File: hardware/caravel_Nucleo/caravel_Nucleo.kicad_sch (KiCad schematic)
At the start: 65 parts, among them J1 10118193-0001LF, J10 PinHeader_1x11, J11 PinHeader_1x02, J12 PinHeader_1x02, J3 PinHeader_1x02, J4 836-22-004-10-001101, J5 PinHeader_1x02, J6 PinHeader_1x02, J7 836-22-006-10-001101, J8 640456-3, J9 640456-3, SW1 KMR2, T1 Logo, T2 Logo, U10 MCP4661, U12 NUCLEO144-F746ZG, U4 MAX811REUS+T, U5 TAR5S33UTE85LF, U6 TAR5S18U(TE85L,F), U7 W25Q32FVSS, U8 caravel_breakout, U9 MIC2211-AAYML-TR, X1 ECS-2520MVLC-100-BN-TR

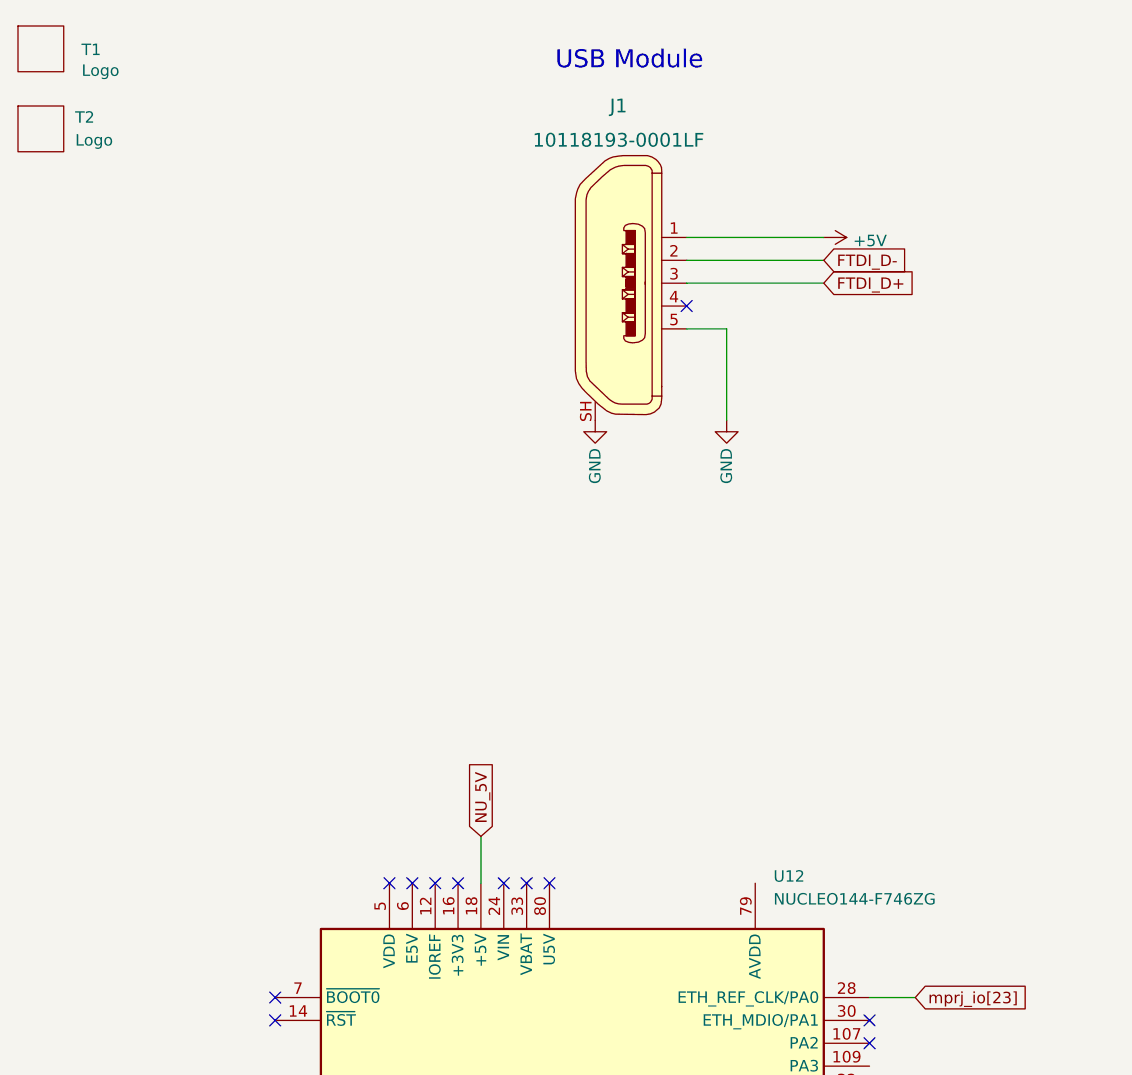
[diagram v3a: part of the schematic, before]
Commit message: Move components to local library
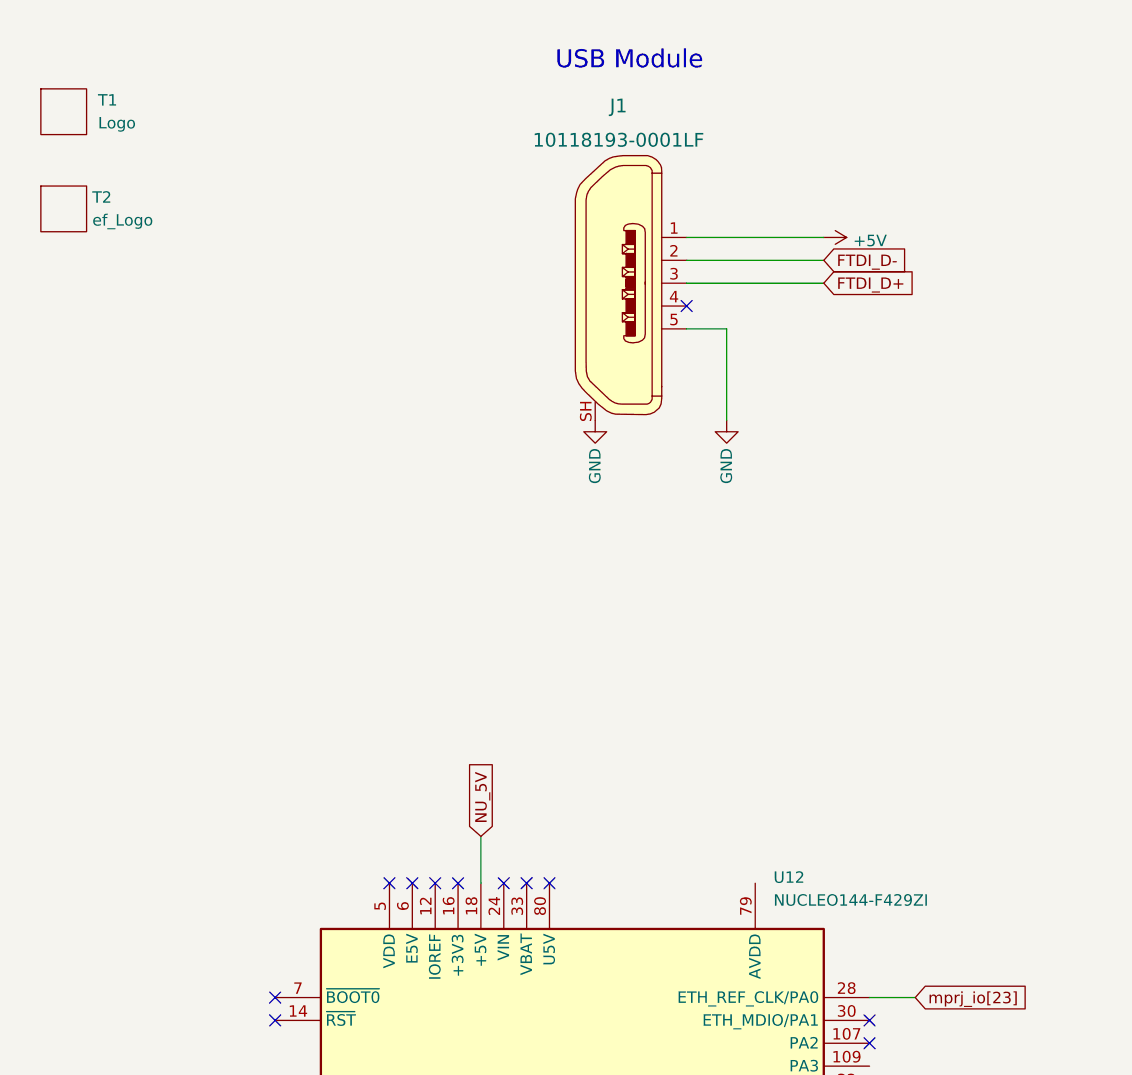
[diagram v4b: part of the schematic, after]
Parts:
- removed T1: Logo, Caravel_Board:logo, symbol Caravel_board:Logo
- removed T2: Logo, Caravel_Board:ef_logo, symbol Caravel_board:Logo
- removed U12: NUCLEO144-F746ZG, Module:ST_Morpho_Connector_144_STLink, symbol MCU_Module:NUCLEO144-F746ZG
- added T1: Logo, caravel_Nucleo-footprints:logo, symbol caravel_Nucleo:Logo
- added T2: ef_Logo, caravel_Nucleo-footprints:ef_logo, symbol caravel_Nucleo:ef_Logo
- added U12: NUCLEO144-F429ZI, caravel_Nucleo-footprints:ST_Morpho_Connectors_144, symbol caravel_Nucleo:NUCLEO144-F429ZI
- C10, C13, C18, C20, C21: footprint antmicro-footprints:0603-cap -> caravel_Nucleo-footprints:0603-cap; symbol antmicroCapacitors0603:C_1u_0603 -> caravel_Nucleo:C_1u_0603
- C11, C14, C19: footprint antmicro-footprints:0603-cap -> caravel_Nucleo-footprints:0603-cap; symbol antmicroCapacitors0603:C_10n_0603 -> caravel_Nucleo:C_10n_0603
- C12, C15: footprint antmicro-footprints:0603-cap -> caravel_Nucleo-footprints:0603-cap; symbol antmicroCapacitors0603:C_10u_0603 -> caravel_Nucleo:C_10u_0603
- C16, C17, C9: footprint antmicro-footprints:0603-cap -> caravel_Nucleo-footprints:0603-cap; symbol antmicroCapacitors0603:C_100n_0603 -> caravel_Nucleo:C_100n_0603
- D3, D4: footprint antmicro-footprints:LED-1206 -> caravel_Nucleo-footprints:LED-1206; symbol antmicroLEDIndicationDiscrete:LTST-C150KGKT -> caravel_Nucleo:LTST-C150KGKT
- J1: footprint antmicro-footprints:USB_Micro_B_Female_10118193-0001LF -> caravel_Nucleo-footprints:USB_Micro_B_Female_10118193-0001LF; symbol antmicroUSBDVIHDMIConnectors:10118193-0001LF -> caravel_Nucleo:10118193-0001LF
- J10: footprint antmicro-footprints:PinHeader_1x11_P2.54_Vertical -> caravel_Nucleo-footprints:PinHeader_1x11_P2.54_Vertical; symbol antmicroRectangularConnectorsHeadersMalePins:PinHeader_1x11 -> caravel_Nucleo:PinHeader_1x11
- J11, J12, J3, J5, J6: footprint antmicro-footprints:PinHeader_1x2_P2.54mm -> caravel_Nucleo-footprints:PinHeader_1x2_P2.54mm; symbol antmicroRectangularConnectorsHeadersMalePins:PinHeader_1x02 -> caravel_Nucleo:PinHeader_1x02
- J4: footprint antmicro-footprints:PogoPinHeader_1x4_P2mm_Drill1,5mm -> caravel_Nucleo-footprints:PogoPinHeader_1x4_P2mm_Drill1,5mm; symbol antmicroRectangularConnectorsHeadersMalePins:836-22-004-10-001101 -> caravel_Nucleo:836-22-004-10-001101
- J7: footprint antmicro-footprints:PogoPinHeader_1x6_P2mm_Drill1,5mm -> caravel_Nucleo-footprints:PogoPinHeader_1x6_P2mm_Drill1,5mm; symbol antmicroRectangularConnectorsHeadersMalePins:836-22-006-10-001101 -> caravel_Nucleo:836-22-006-10-001101
- J8, J9: footprint antmicro-footprints:PinHeader_1x3_P2.54_Drill1.1mm -> caravel_Nucleo-footprints:PinHeader_1x3_P2.54_Drill1.1mm; symbol antmicroRectangularConnectorsHeadersMalePins:640456-3 -> caravel_Nucleo:640456-3
- R10, R11, R12, R15, R16, R17, R18, R27, R7, R8, R9: footprint antmicro-footprints:0603-res -> caravel_Nucleo-footprints:0603-res; symbol antmicroResistors0603:R_10k_0603 -> caravel_Nucleo:R_10k_0603
- R13, R14: footprint antmicro-footprints:0603-res -> caravel_Nucleo-footprints:0603-res; symbol antmicroResistors0603:R_82R_0603 -> caravel_Nucleo:R_82R_0603
- R19: footprint antmicro-footprints:0603-res -> caravel_Nucleo-footprints:0603-res; symbol antmicroResistors0603:R_360R_0603 -> caravel_Nucleo:R_360R_0603
- R20, R23: footprint antmicro-footprints:0603-res -> caravel_Nucleo-footprints:0603-res; symbol antmicroResistors0603:R_4k99_0603 -> caravel_Nucleo:R_4k99_0603
- R21: footprint antmicro-footprints:0603-res -> caravel_Nucleo-footprints:0603-res; symbol antmicroResistors0603:R_499R_0603 -> caravel_Nucleo:R_499R_0603
- R22: footprint antmicro-footprints:0603-res -> caravel_Nucleo-footprints:0603-res; symbol antmicroResistors0603:R_4k22_0603 -> caravel_Nucleo:R_4k22_0603
- R24: footprint antmicro-footprints:0402-res -> caravel_Nucleo-footprints:0402-res; symbol antmicroResistors0402:R_4k02_0402 -> caravel_Nucleo:R_4k02_0402
- R25, R26: footprint antmicro-footprints:0603-res -> caravel_Nucleo-footprints:0603-res; symbol antmicroResistors0603:R_4k7_0603 -> caravel_Nucleo:R_4k7_0603
- R29, R30, R31, R32, R33: footprint antmicro-footprints:0603-res -> caravel_Nucleo-footprints:0603-res; symbol antmicroResistors0603:R_0R_0603 -> caravel_Nucleo:R_0R_0603
- SW1: footprint antmicro-footprints:SW_SPST_4.2x2.8 -> caravel_Nucleo-footprints:SW_SPST_4.2x2.8; symbol antmicroPushbuttonSwitches:KMR2 -> caravel_Nucleo:KMR2
- TP1: footprint antmicro-footprints:Testpoint_smd_1mm -> caravel_Nucleo-footprints:Testpoint_smd_1mm; symbol antmicroTestPoints:TP_SMD1MM -> caravel_Nucleo:TP_SMD1MM
- U10: footprint antmicro-footprints:QFN-16_EP_4x4_Pitch0.65mm -> caravel_Nucleo-footprints:QFN-16_EP_4x4_Pitch0.65mm; symbol antmicroInterfaceIOExpanders:MCP4661 -> caravel_Nucleo:MCP4661
- U4: footprint antmicro-footprints:SOT-143-4 -> caravel_Nucleo-footprints:SOT-143-4; symbol antmicroPMICPowerSequencers:MAX811REUS+T -> caravel_Nucleo:MAX811REUS+T
- U5: footprint antmicro-footprints:SOT-353 -> caravel_Nucleo-footprints:SOT-353; symbol antmicroPMICVoltageRegulatorsLinear:TAR5S33UTE85LF -> caravel_Nucleo:TAR5S33UTE85LF
- U6: footprint antmicro-footprints:SOT-353 -> caravel_Nucleo-footprints:SOT-353; symbol antmicroPMICVoltageRegulatorsLinear:TAR5S18U(TE85L,F) -> caravel_Nucleo:TAR5S18U(TE85L,F)
- U7: footprint antmicro-footprints:SOIC127P790X216-8N -> caravel_Nucleo-footprints:SOIC127P790X216-8N; symbol antmicroMemory:W25Q32FVSS -> caravel_Nucleo:W25Q32FVSS
- U8: footprint antmicro-footprints:caravel_breakout -> caravel_Nucleo-footprints:caravel_breakout; symbol antmicroModules:caravel_breakout -> caravel_Nucleo:caravel_breakout
- U9: footprint antmicro-footprints:DFN-10-1EP_3x3mm -> caravel_Nucleo-footprints:DFN-10-1EP_3x3mm; symbol antmicroPMICVoltageRegulatorsLinear:MIC2211-AAYML-TR -> caravel_Nucleo:MIC2211-AAYML-TR
- X1: footprint antmicro-footprints:Oscillator_SMD_ECS_2520MV-xxx-xx-4Pin_2.5x2.0mm -> caravel_Nucleo-footprints:Oscillator_SMD_ECS_2520MV-xxx-xx-4Pin_2.5x2.0mm; symbol antmicroCrystals:ECS-2520MVLC-100-BN-TR -> caravel_Nucleo:ECS-2520MVLC-100-BN-TR
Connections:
- net EN_VOUT1: now also U12.52 (PF2)
- net EN_VOUT2: now also U12.47 (PE3)
- net GND: now also U12.104 (AGND), U12.111 (GND), U12.126 (GND), U12.135 (GND), U12.143 (GND), U12.144 (GND), U12.19 (GND), U12.20 (GND), U12.22 (GND), U12.49 (GND), U12.60 (GND), U12.71 (GND), U12.72 (GND), U12.8 (GND), U12.81 (GND), U12.92 (GND)
- net I2C4_SCL: now also U12.115 (PD12)
- net I2C4_SDA: now also U12.113 (PD13)
- net NU_5V: now also U12.18 (+5V)
- net SPI4_CS: now also U12.128 (PE11)
- net SPI4_MISO: now also U12.127 (PE13)
- net SPI4_MOSI: now also U12.123 (PE14)
- net SPI4_SCK: now also U12.121 (PE12)
- net SPI5_CS: now also U12.9 (PF6)
- net SPI5_MISO: now also U12.54 (PF8)
- net SPI5_MOSI: now also U12.56 (PF9)
- net SPI5_SCK: now also U12.11 (PF7)
- net TIM3_CH2: now also U12.101 (PB5)
- net UART8_RX: now also U12.136 (PE0)
- net UART8_TX: now also U12.61 (PE1)
- net mprj_io[0]: now also U12.65 (PG12)
- net mprj_io[10]: now also U12.59 (PG0)
- net mprj_io[11]: now also U12.58 (PG1)
- net mprj_io[12]: now also U12.45 (PD7)
- net mprj_io[13]: now also U12.44 (PG3)
- net mprj_io[14]: now also U12.43 (PD6)
- net mprj_io[15]: now also U12.42 (PG2)
- net mprj_io[16]: now also U12.41 (PD5)
- net mprj_io[17]: now also U12.40 (PD3)
- net mprj_io[18]: now also U12.39 (PD4)
- net mprj_io[19]: now also U12.38 (PC0)
- net mprj_io[20]: now also U12.37 (PC3)
- net mprj_io[21]: now also U12.35 (PC2)
- net mprj_io[22]: now also U12.32 (PA4)
- net mprj_io[23]: now also U12.28 (ETH_REF_CLK/PA0)
- net mprj_io[24]: now also U12.17 (PA15)
- net mprj_io[25]: now also U12.1 (PC10)
- net mprj_io[26]: now also U12.2 (PC11)
- net mprj_io[27]: now also U12.4 (PD2)
- net mprj_io[28]: now also U12.73 (PC9)
- net mprj_io[29]: now also U12.74 (PC8)
- net mprj_io[30]: now also U12.75 (PB8)
- net mprj_io[31]: now also U12.76 (PC6)
- net mprj_io[32]: now also U12.77 (PB9)
- net mprj_io[33]: now also U12.88 (PB12)
- net mprj_io[34]: now also U12.89 (PB6)
- net mprj_io[35]: now also U12.94 (PB2)
- net mprj_io[36]: now also U12.96 (PB1)
- net mprj_io[37]: now also U12.98 (PB15)
- net mprj_io[7]: now also U12.66 (PG10)
- net mprj_io[8]: now also U12.64 (PG15)
- net mprj_io[9]: now also U12.63 (PG9)
- net ~{MR}: now also U12.3 (PC12)

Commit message: Rework FTDI sheet, begin improving main schematic sheet
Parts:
- removed J1: 10118193-0001LF, caravel_Nucleo-footprints:USB_Micro_B_Female_10118193-0001LF, symbol caravel_Nucleo:10118193-0001LF
- removed T1: Logo, caravel_Nucleo-footprints:logo, symbol caravel_Nucleo:Logo
- removed T2: ef_Logo, caravel_Nucleo-footprints:ef_logo, symbol caravel_Nucleo:ef_Logo
- removed U12: NUCLEO144-F429ZI, caravel_Nucleo-footprints:ST_Morpho_Connectors_144, symbol caravel_Nucleo:NUCLEO144-F429ZI
- added T1: Logo, Caravel_Board:logo, symbol Caravel_board:Logo
- added T2: Logo, Caravel_Board:ef_logo, symbol Caravel_board:Logo
- added U12: NUCLEO144-F746ZG, Module:ST_Morpho_Connector_144_STLink, symbol MCU_Module:NUCLEO144-F746ZG
- C10, C13, C18, C20, C21: footprint caravel_Nucleo-footprints:0603-cap -> antmicro-footprints:0603-cap; symbol caravel_Nucleo:C_1u_0603 -> antmicroCapacitors0603:C_1u_0603
- C11, C14, C19: footprint caravel_Nucleo-footprints:0603-cap -> antmicro-footprints:0603-cap; symbol caravel_Nucleo:C_10n_0603 -> antmicroCapacitors0603:C_10n_0603
- C12, C15: footprint caravel_Nucleo-footprints:0603-cap -> antmicro-footprints:0603-cap; symbol caravel_Nucleo:C_10u_0603 -> antmicroCapacitors0603:C_10u_0603
- C16, C17, C9: footprint caravel_Nucleo-footprints:0603-cap -> antmicro-footprints:0603-cap; symbol caravel_Nucleo:C_100n_0603 -> antmicroCapacitors0603:C_100n_0603
- D3, D4: footprint caravel_Nucleo-footprints:LED-1206 -> antmicro-footprints:LED-1206; symbol caravel_Nucleo:LTST-C150KGKT -> antmicroLEDIndicationDiscrete:LTST-C150KGKT
- J10: footprint caravel_Nucleo-footprints:PinHeader_1x11_P2.54_Vertical -> antmicro-footprints:PinHeader_1x11_P2.54_Vertical; symbol caravel_Nucleo:PinHeader_1x11 -> antmicroRectangularConnectorsHeadersMalePins:PinHeader_1x11
- J11, J12, J3, J5, J6: footprint caravel_Nucleo-footprints:PinHeader_1x2_P2.54mm -> antmicro-footprints:PinHeader_1x2_P2.54mm; symbol caravel_Nucleo:PinHeader_1x02 -> antmicroRectangularConnectorsHeadersMalePins:PinHeader_1x02
- J4: footprint caravel_Nucleo-footprints:PogoPinHeader_1x4_P2mm_Drill1,5mm -> antmicro-footprints:PogoPinHeader_1x4_P2mm_Drill1,5mm; symbol caravel_Nucleo:836-22-004-10-001101 -> antmicroRectangularConnectorsHeadersMalePins:836-22-004-10-001101
- J7: footprint caravel_Nucleo-footprints:PogoPinHeader_1x6_P2mm_Drill1,5mm -> antmicro-footprints:PogoPinHeader_1x6_P2mm_Drill1,5mm; symbol caravel_Nucleo:836-22-006-10-001101 -> antmicroRectangularConnectorsHeadersMalePins:836-22-006-10-001101
- J8, J9: footprint caravel_Nucleo-footprints:PinHeader_1x3_P2.54_Drill1.1mm -> antmicro-footprints:PinHeader_1x3_P2.54_Drill1.1mm; symbol caravel_Nucleo:640456-3 -> antmicroRectangularConnectorsHeadersMalePins:640456-3
- R10, R11, R12, R15, R16, R17, R18, R27, R7, R8, R9: footprint caravel_Nucleo-footprints:0603-res -> antmicro-footprints:0603-res; symbol caravel_Nucleo:R_10k_0603 -> antmicroResistors0603:R_10k_0603
- R13, R14: footprint caravel_Nucleo-footprints:0603-res -> antmicro-footprints:0603-res; symbol caravel_Nucleo:R_82R_0603 -> antmicroResistors0603:R_82R_0603
- R19: footprint caravel_Nucleo-footprints:0603-res -> antmicro-footprints:0603-res; symbol caravel_Nucleo:R_360R_0603 -> antmicroResistors0603:R_360R_0603
- R20, R23: footprint caravel_Nucleo-footprints:0603-res -> antmicro-footprints:0603-res; symbol caravel_Nucleo:R_4k99_0603 -> antmicroResistors0603:R_4k99_0603
- R21: footprint caravel_Nucleo-footprints:0603-res -> antmicro-footprints:0603-res; symbol caravel_Nucleo:R_499R_0603 -> antmicroResistors0603:R_499R_0603
- R22: footprint caravel_Nucleo-footprints:0603-res -> antmicro-footprints:0603-res; symbol caravel_Nucleo:R_4k22_0603 -> antmicroResistors0603:R_4k22_0603
- R24: footprint caravel_Nucleo-footprints:0402-res -> antmicro-footprints:0402-res; symbol caravel_Nucleo:R_4k02_0402 -> antmicroResistors0402:R_4k02_0402
- R25, R26: footprint caravel_Nucleo-footprints:0603-res -> antmicro-footprints:0603-res; symbol caravel_Nucleo:R_4k7_0603 -> antmicroResistors0603:R_4k7_0603
- R29, R30, R31, R32, R33: footprint caravel_Nucleo-footprints:0603-res -> antmicro-footprints:0603-res; symbol caravel_Nucleo:R_0R_0603 -> antmicroResistors0603:R_0R_0603
- SW1: footprint caravel_Nucleo-footprints:SW_SPST_4.2x2.8 -> antmicro-footprints:SW_SPST_4.2x2.8; symbol caravel_Nucleo:KMR2 -> antmicroPushbuttonSwitches:KMR2
- TP1: footprint caravel_Nucleo-footprints:Testpoint_smd_1mm -> antmicro-footprints:Testpoint_smd_1mm; symbol caravel_Nucleo:TP_SMD1MM -> antmicroTestPoints:TP_SMD1MM
- U10: footprint caravel_Nucleo-footprints:QFN-16_EP_4x4_Pitch0.65mm -> antmicro-footprints:QFN-16_EP_4x4_Pitch0.65mm; symbol caravel_Nucleo:MCP4661 -> antmicroInterfaceIOExpanders:MCP4661
- U4: footprint caravel_Nucleo-footprints:SOT-143-4 -> antmicro-footprints:SOT-143-4; symbol caravel_Nucleo:MAX811REUS+T -> antmicroPMICPowerSequencers:MAX811REUS+T
- U5: footprint caravel_Nucleo-footprints:SOT-353 -> antmicro-footprints:SOT-353; symbol caravel_Nucleo:TAR5S33UTE85LF -> antmicroPMICVoltageRegulatorsLinear:TAR5S33UTE85LF
- U6: footprint caravel_Nucleo-footprints:SOT-353 -> antmicro-footprints:SOT-353; symbol caravel_Nucleo:TAR5S18U(TE85L,F) -> antmicroPMICVoltageRegulatorsLinear:TAR5S18U(TE85L,F)
- U7: footprint caravel_Nucleo-footprints:SOIC127P790X216-8N -> antmicro-footprints:SOIC127P790X216-8N; symbol caravel_Nucleo:W25Q32FVSS -> antmicroMemory:W25Q32FVSS
- U8: footprint caravel_Nucleo-footprints:caravel_breakout -> antmicro-footprints:caravel_breakout; symbol caravel_Nucleo:caravel_breakout -> antmicroModules:caravel_breakout
- U9: footprint caravel_Nucleo-footprints:DFN-10-1EP_3x3mm -> antmicro-footprints:DFN-10-1EP_3x3mm; symbol caravel_Nucleo:MIC2211-AAYML-TR -> antmicroPMICVoltageRegulatorsLinear:MIC2211-AAYML-TR
- X1: footprint caravel_Nucleo-footprints:Oscillator_SMD_ECS_2520MV-xxx-xx-4Pin_2.5x2.0mm -> antmicro-footprints:Oscillator_SMD_ECS_2520MV-xxx-xx-4Pin_2.5x2.0mm; symbol caravel_Nucleo:ECS-2520MVLC-100-BN-TR -> antmicroCrystals:ECS-2520MVLC-100-BN-TR
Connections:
- net EN_VOUT1: now also U12.52 (PF2)
- net EN_VOUT2: now also U12.47 (PE3)
- net GND: now also U12.104 (AGND), U12.111 (GND), U12.126 (GND), U12.135 (GND), U12.143 (GND), U12.144 (GND), U12.19 (GND), U12.20 (GND), U12.22 (GND), U12.49 (GND), U12.60 (GND), U12.71 (GND), U12.72 (GND), U12.8 (GND), U12.81 (GND), U12.92 (GND)
- net I2C4_SCL: now also U12.115 (PD12)
- net I2C4_SDA: now also U12.113 (PD13)
- net NU_5V: now also U12.18 (+5V)
- net SPI4_CS: now also U12.128 (PE11)
- net SPI4_MISO: now also U12.127 (PE13)
- net SPI4_MOSI: now also U12.123 (PE14)
- net SPI4_SCK: now also U12.121 (PE12)
- net SPI5_CS: now also U12.9 (PF6)
- net SPI5_MISO: now also U12.54 (PF8)
- net SPI5_MOSI: now also U12.56 (PF9)
- net SPI5_SCK: now also U12.11 (PF7)
- net TIM3_CH2: now also U12.101 (PB5)
- net UART8_RX: now also U12.136 (PE0)
- net UART8_TX: now also U12.61 (PE1)
- net mprj_io[0]: now also U12.65 (PG12)
- net mprj_io[10]: now also U12.59 (PG0)
- net mprj_io[11]: now also U12.58 (PG1)
- net mprj_io[12]: now also U12.45 (PD7)
- net mprj_io[13]: now also U12.44 (PG3)
- net mprj_io[14]: now also U12.43 (PD6)
- net mprj_io[15]: now also U12.42 (PG2)
- net mprj_io[16]: now also U12.41 (PD5)
- net mprj_io[17]: now also U12.40 (PD3)
- net mprj_io[18]: now also U12.39 (PD4)
- net mprj_io[19]: now also U12.38 (PC0)
- net mprj_io[20]: now also U12.37 (PC3)
- net mprj_io[21]: now also U12.35 (PC2)
- net mprj_io[22]: now also U12.32 (PA4)
- net mprj_io[23]: now also U12.28 (ETH_REF_CLK/PA0)
- net mprj_io[24]: now also U12.17 (PA15)
- net mprj_io[25]: now also U12.1 (PC10)
- net mprj_io[26]: now also U12.2 (PC11)
- net mprj_io[27]: now also U12.4 (PD2)
- net mprj_io[28]: now also U12.73 (PC9)
- net mprj_io[29]: now also U12.74 (PC8)
- net mprj_io[30]: now also U12.75 (PB8)
- net mprj_io[31]: now also U12.76 (PC6)
- net mprj_io[32]: now also U12.77 (PB9)
- net mprj_io[33]: now also U12.88 (PB12)
- net mprj_io[34]: now also U12.89 (PB6)
- net mprj_io[35]: now also U12.94 (PB2)
- net mprj_io[36]: now also U12.96 (PB1)
- net mprj_io[37]: now also U12.98 (PB15)
- net mprj_io[7]: now also U12.66 (PG10)
- net mprj_io[8]: now also U12.64 (PG15)
- net mprj_io[9]: now also U12.63 (PG9)
- net ~{MR}: now also U12.3 (PC12)
- net V1.8 renamed 1V8
- net V3.3 renamed 3V3
- no-connect marks 36 -> 35
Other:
- note removed: "USB Module"
- moved on the sheet: J10, J4, J7
